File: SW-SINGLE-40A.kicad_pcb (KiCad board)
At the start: 2 copper layers, 63 x 69 mm, 20 parts, among them J1 CTL, U1 BTS50010-1TAD

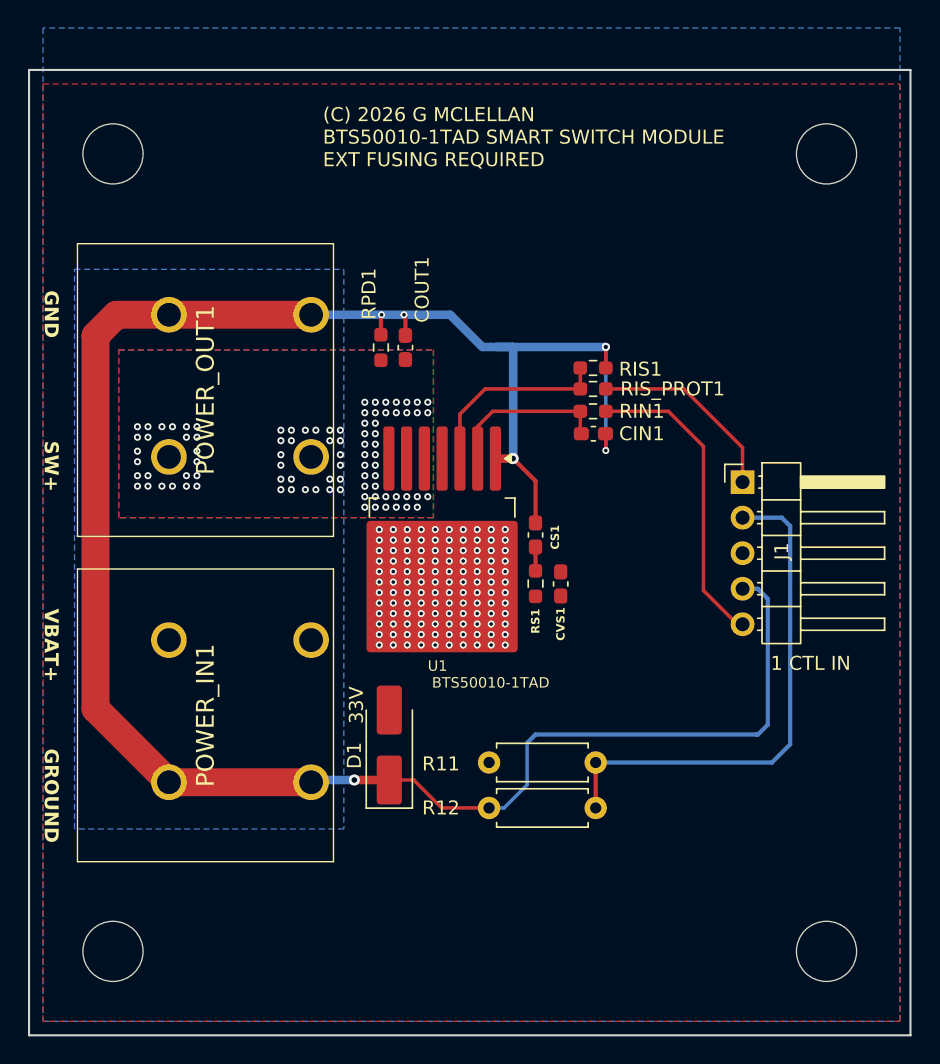
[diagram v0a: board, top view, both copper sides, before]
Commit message: layout and silkscreen tweaks
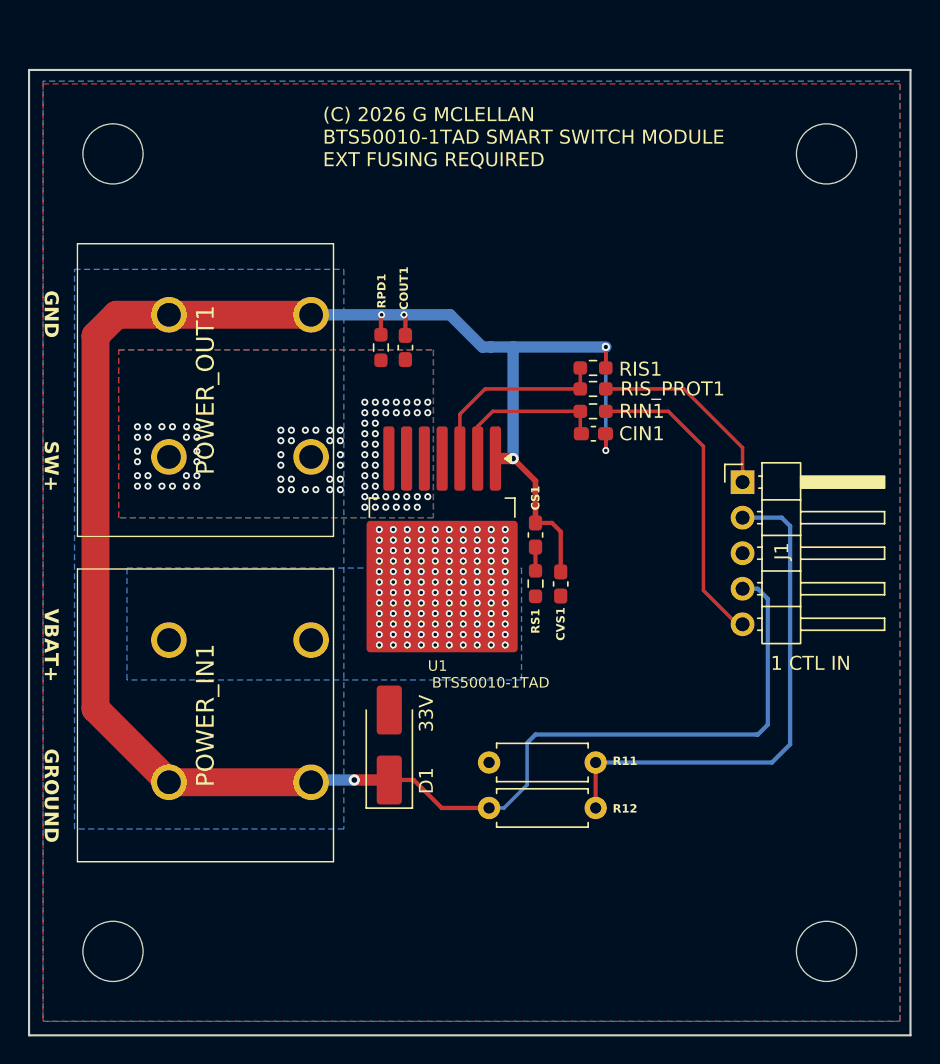
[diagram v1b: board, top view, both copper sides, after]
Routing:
- net GND: track 159.9 -> 164.9 mm
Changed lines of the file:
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@@
 		(tags "resistor handsolder")
 		(property "Reference" "RPD1"
-			(at -3.8375 0.85 90)
+			(at -4.0375 -0.05 90)
 			(layer "F.SilkS")
 			(effects
 				(font
-					(size 1 1)
-					(thickness 0.15)
+					(size 0.6 0.6)
+					(thickness 0.1)
+					(bold yes)
 				)
 			)
@@
 		(tags "capacitor handsolder")
 		(property "Reference" "COUT1"
-			(at 4.1375 1.2 90)
+			(at 4.2375 -0.1 90)
 			(layer "F.SilkS")
 			(effects
 				(font
-					(size 1 1)
-					(thickness 0.15)
+					(size 0.6 0.6)
+					(thickness 0.1)
+					(bold yes)
 				)
 			)
@@
 		(tags "Resistor Axial_DIN0207 series Axial Horizontal pin pitch 7.62mm 0.25W = 1/4W length 6.3mm diameter 2.5mm")
 		(property "Reference" "R11"
-			(at 11.06 -0.1 0)
+			(at -2.1 0.1 0)
 			(layer "F.SilkS")
 			(effects
 				(font
-					(size 1 1)
-					(thickness 0.15)
+					(size 0.6 0.6)
+					(thickness 0.1)
+					(bold yes)
 				)
 			)
@@
 		(tags "Resistor Axial_DIN0207 series Axial Horizontal pin pitch 7.62mm 0.25W = 1/4W length 6.3mm diameter 2.5mm")
 		(property "Reference" "R12"
-			(at -3.44 0 0)
+			(at 9.72 0.05 0)
 			(layer "F.SilkS")
 			(effects
 				(font
-					(size 1 1)
-					(thickness 0.15)
+					(size 0.6 0.6)
+					(thickness 0.1)
+					(bold yes)
 				)
 			)
@@
 		(tags "Diode SMA (DO-214AC) Handsoldering")
 		(property "Reference" "D1"
-			(at -0.75 -2.5 90)
+			(at -2.55 2.65 90)
 			(layer "F.SilkS")
 			(effects
@@
 		)
 		(property "Value" "33V"
-			(at 2.85 -2.35 90)
+			(at 2.25 2.65 90)
 			(layer "F.SilkS")
 			(effects
@@
 		(tags "capacitor handsolder")
 		(property "Reference" "CS1"
-			(at -0.1625 1.4 90)
+			(at 2.6375 0 90)
 			(layer "F.SilkS")
 			(effects
@@
 	)
 	(segment
+		(start 126.2 98.375)
+		(end 127.375 98.375)
+		(width 0.305)
+		(layer "F.Cu")
+		(net 1)
+	)
+	(segment
 		(start 131.225 92.025)
 		(end 131.2 92)
@@
 	)
 	(segment
+		(start 128 99)
+		(end 128 101.875)
+		(width 0.305)
+		(layer "F.Cu")
+		(net 1)
+	)
+	(segment
 		(start 131.225 87.3)
 		(end 131.225 85.8)
@@
 		(start 117.5 116.75)
 		(end 119.5 118.75)
-		(width 0.254)
+		(width 0.305)
 		(layer "F.Cu")
 		(net 1)
@@
 		(start 115.75 116.75)
 		(end 113.25 116.75)
-		(width 0.61)
+		(width 0.8128)
 		(layer "F.Cu")
 		(net 1)
@@
 		(start 115.75 116.75)
 		(end 117.5 116.75)
-		(width 0.254)
+		(width 0.305)
 		(layer "F.Cu")
 		(net 1)
@@
 		(start 124.6 93.775)
 		(end 123.335 93.775)
-		(width 0.61)
+		(width 0.8128)
 		(layer "F.Cu")
 		(net 1)
@@
 		(start 119.5 118.75)
 		(end 122.88 118.75)
-		(width 0.254)
+		(width 0.305)
 		(layer "F.Cu")
 		(net 1)
@@
 	)
 	(segment
+		(start 127.375 98.375)
+		(end 128 99)
+		(width 0.305)
+		(layer "F.Cu")
+		(net 1)
+	)
+	(segment
 		(start 116.9 83.6)
 		(end 116.8 83.5)
@@
 		(start 126.2 98.375)
 		(end 126.2 95.375)
-		(width 0.305)
+		(width 0.406)
 		(layer "F.Cu")
 		(net 1)
@@
 		(start 126.2 95.375)
 		(end 124.6 93.775)
-		(width 0.305)
+		(width 0.406)
 		(layer "F.Cu")
 		(net 1)
@@
 		(start 122.4 85.8)
 		(end 120.1 83.5)
-		(width 0.61)
+		(width 0.8128)
 		(layer "B.Cu")
 		(net 1)
@@
 		(start 124.6 85.8)
 		(end 124.6 93.775)
-		(width 0.61)
+		(width 0.8128)
 		(layer "B.Cu")
 		(net 1)
@@
 		(start 120.1 83.5)
 		(end 110.16 83.5)
-		(width 0.61)
+		(width 0.8128)
 		(layer "B.Cu")
 		(net 1)
@@
 		(start 131.225 85.8)
 		(end 123 85.8)
-		(width 0.61)
+		(width 0.8128)
 		(layer "B.Cu")
 		(net 1)
@@
 		(start 123 85.8)
 		(end 122.4 85.8)
-		(width 0.61)
+		(width 0.8128)
 		(layer "B.Cu")
 		(net 1)
@@
 		(start 113.25 116.75)
 		(end 110.32 116.75)
-		(width 0.61)
+		(width 0.8128)
 		(layer "B.Cu")
 		(net 1)
@@
 		(polygon
 			(pts
-				(xy 152.25 63) (xy 91 63) (xy 91 134) (xy 152.25 134)
+				(xy 152.25 66.8) (xy 91 66.8) (xy 91 134) (xy 152.25 134)
+			)
+		)
+	)
+	(zone
+		(net 5)
+		(net_name "+12V")
+		(layer "B.Cu")
+		(name "PWRIN")
+		(hatch edge 0.5)
+		(priority 3)
+		(connect_pads yes
+			(clearance 0.18)
+		)
+		(min_thickness 0.254)
+		(filled_areas_thickness no)
+		(fill yes
+			(thermal_gap 0.5)
+			(thermal_bridge_width 0.5)
+			(smoothing fillet)
+			(radius 2)
+		)
+		(polygon
+			(pts
+				(xy 97 101.6) (xy 125.2 101.6) (xy 125.2 109.6) (xy 97 109.6)
 			)
 		)
